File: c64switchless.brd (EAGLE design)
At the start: 22.8 x 44.1 mm, 12 parts, among them IC1 27C256, IC2 PIC12F629P, X1 B4B-ZR

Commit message: Revision + silkscreen text
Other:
- board text added: "B"
- board text added: "G"
- board text added: "Gnd"
- board text added: "LED"
- board text added: "R"
- board text added: "Revision 1"
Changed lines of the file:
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@@
 <setting verticaltext="up"/>
 </settings>
-<grid distance="0.05" unitdist="inch" unit="mm" style="lines" multiple="1" display="yes" altdistance="0.025" altunitdist="inch" altunit="inch"/>
+<grid distance="0.05" unitdist="inch" unit="inch" style="lines" multiple="1" display="yes" altdistance="0.025" altunitdist="inch" altunit="inch"/>
 <layers>
 <layer number="1" name="Top" color="4" fill="1" visible="yes" active="yes"/>
@@
 <text x="1.27" y="1.27" size="0.6096" layer="29" font="fixed">Quad Kernal Switch</text>
 <text x="5.715" y="5.5" size="0.6096" layer="21" rot="R340">RESET</text>
-<text x="11.43" y="0.5" size="0.6096" layer="21" rot="R70">Restore</text>
+<text x="13.335" y="3.04" size="0.6096" layer="21" rot="R70">Restore</text>
+<text x="13.97" y="1.27" size="0.6096" layer="23" font="fixed" rot="R90">LED</text>
+<text x="3.175" y="0.635" size="0.6096" layer="23" font="fixed">Revision 1</text>
+<text x="19.812" y="0.635" size="0.6096" layer="23" font="fixed">R</text>
+<text x="16.764" y="0.635" size="0.6096" layer="23" font="fixed">G</text>
+<text x="15.24" y="0.635" size="0.6096" layer="23" font="fixed">B</text>
+<text x="17.78" y="0.635" size="0.6096" layer="23" font="fixed">Gnd</text>
 </plain>
 <attributes>

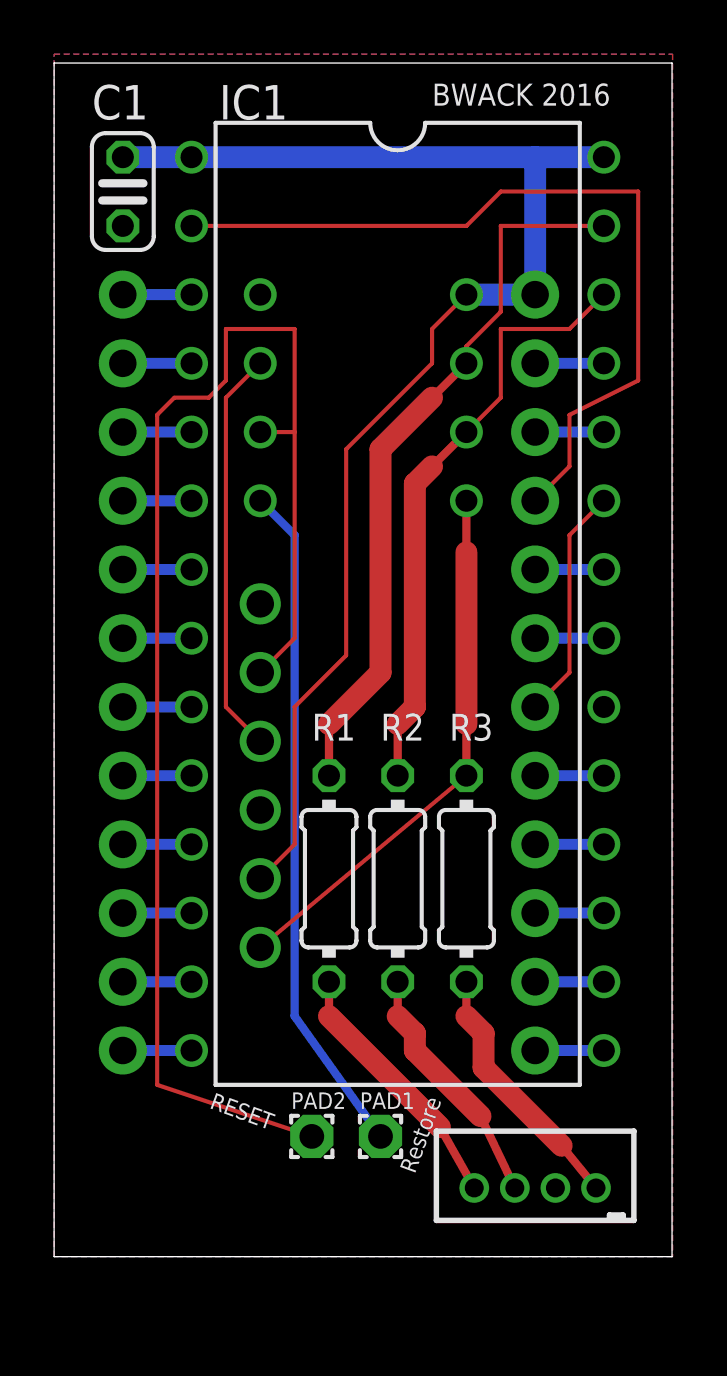
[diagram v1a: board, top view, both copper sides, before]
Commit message: swapped LED and RESTORE on GP2 and GP3
GP3 is the fekken input only pin
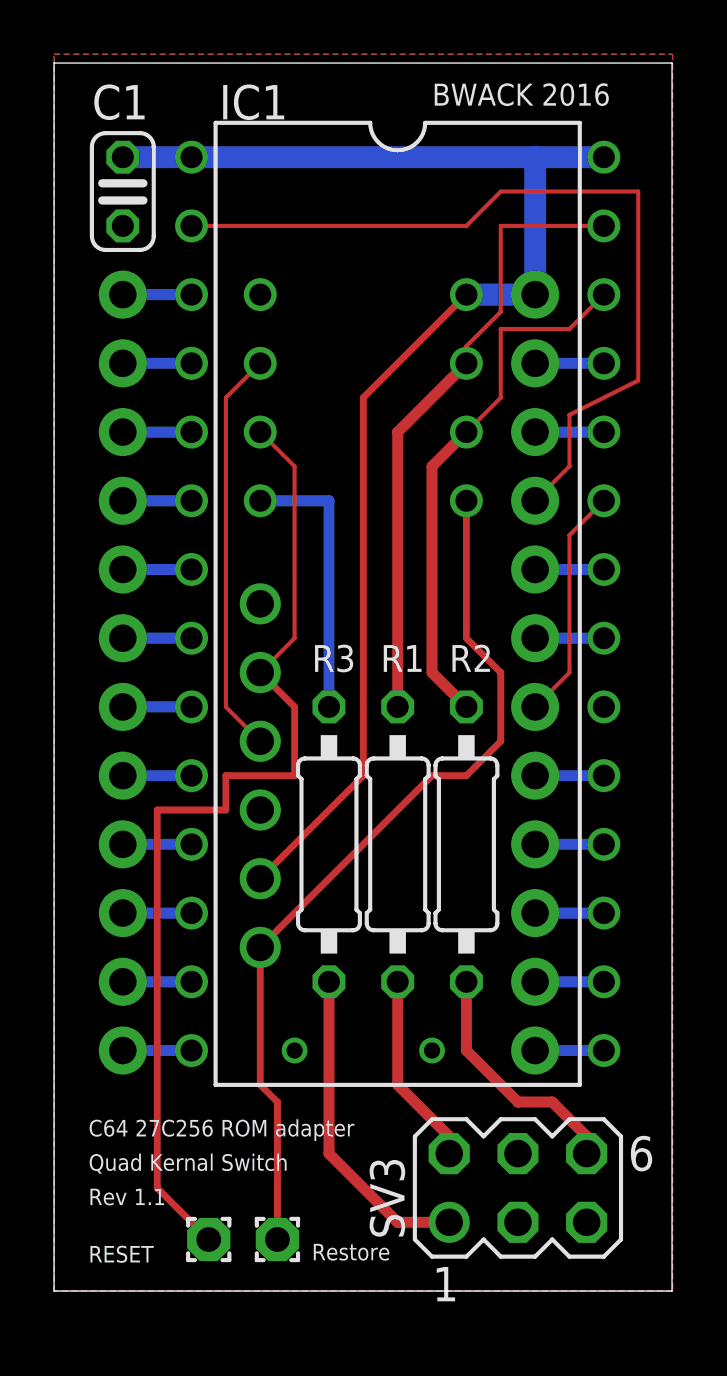
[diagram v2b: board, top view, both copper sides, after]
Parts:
- removed X1: B4B-ZR, con-jst:B4B-ZR
- added SV3: (no value), con-lstb:MA03-2
- R1, R2, R3: value 560 -> 2k; device rcl:0204/7 -> rcl:0207/10
- moved PAD2 5.39 mm to (5.71, 0.64)
- moved PAD1 5.39 mm to (8.26, 0.64)
- moved R3 5.24 mm to (10.2, 15.2)
- moved R2 2.84 mm to (15.2, 15.2)
- moved R1 2.84 mm to (12.7, 15.2)
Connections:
- removed net N$25: IC2.4, R3.2, U$1.1
- new net N$22: IC2.5, R3.2
- net #RESTORE: now also IC2.4, U$1.1; no longer IC2.5
- net BLUE: now also SV3.2; no longer X1.4
- net GND: now also SV3.3, SV3.4; no longer X1.2
- net GREEN: now also SV3.6; no longer X1.3
- net RED: now also SV3.1; no longer X1.1
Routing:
- net N$25: track 20.1 -> 0.00 mm
- net #INTRST: track 52.8 -> 37.3 mm
- net N$22: track 0.00 -> 10.2 mm
- net #RESTORE: track 25.0 -> 32.5 mm
- net A14: track 26.8 -> 23.2 mm
- net A13: track 22.4 -> 19.9 mm
- net BLUE: track 9.65 -> 7.14 mm
- net RED: track 9.53 -> 11.8 mm
- net GND: vias 0 -> 2
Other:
- board size 22.8 x 44.1 mm -> 22.8 x 45.4 mm
- board text added: "C64 27C256 ROM adapter"
- board text added: "Rev 1.1"
- board text removed: "27C256 ROM adapter"
- board text removed: "C64 Longboard"
- board text removed: "Revision 1"

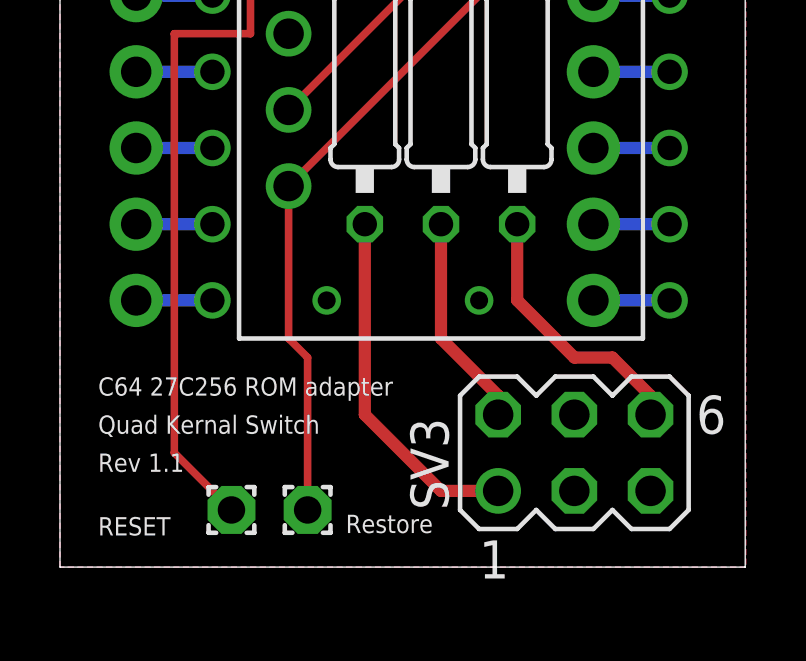
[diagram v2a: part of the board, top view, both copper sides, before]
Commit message: Sch+Layout changed to match RGB LEDs pinout
See readme.txt
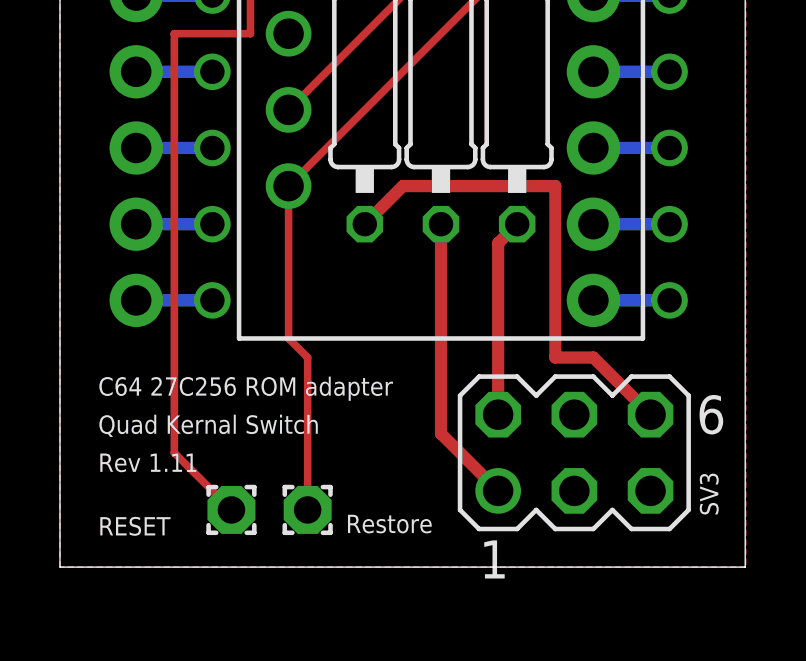
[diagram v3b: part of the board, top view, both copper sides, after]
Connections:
- net BLUE: now also SV3.1; no longer SV3.2
- net GREEN: now also SV3.2; no longer SV3.6
- net RED: now also SV3.6; no longer SV3.1
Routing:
- net RED: track 11.8 -> 16.6 mm
- net BLUE: track 7.14 -> 9.68 mm
- net GREEN: track 8.94 -> 6.61 mm
- net GND: vias 2 -> 0
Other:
- board text added: "BLUE"
- board text added: "GND"
- board text added: "GREEN"
- board text added: "RED"
- board text added: "RGB LEDs"
- board text added: "Rev 1.11"
- board text removed: "B"
- board text removed: "G"
- board text removed: "Gnd"
- board text removed: "LED"
- board text removed: "R"
- board text removed: "Rev 1.1"
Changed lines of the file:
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@@
 <setting verticaltext="up"/>
 </settings>
-<grid distance="0.05" unitdist="inch" unit="inch" style="lines" multiple="1" display="yes" altdistance="0.025" altunitdist="inch" altunit="inch"/>
+<grid distance="0.05" unitdist="inch" unit="inch" style="lines" multiple="1" display="yes" altdistance="0.0125" altunitdist="inch" altunit="inch"/>
 <layers>
 <layer number="1" name="Top" color="4" fill="1" visible="yes" active="yes"/>
@@
 <text x="1.27" y="-0.215" size="0.6096" layer="21">RESET</text>
 <text x="9.525" y="-0.135" size="0.6096" layer="21">Restore</text>
-<text x="13.97" y="1.27" size="0.6096" layer="23" font="fixed" rot="R90">LED</text>
-<text x="1.27" y="1.905" size="0.6096" layer="21" font="fixed">Rev 1.1</text>
-<text x="19.812" y="0.635" size="0.6096" layer="23" font="fixed">R</text>
-<text x="16.764" y="0.635" size="0.6096" layer="23" font="fixed">G</text>
-<text x="15.24" y="0.635" size="0.6096" layer="23" font="fixed">B</text>
-<text x="17.78" y="0.635" size="0.6096" layer="23" font="fixed">Gnd</text>
+<text x="19.05" y="0" size="0.6096" layer="23" font="fixed" rot="R180">RGB LEDs</text>
+<text x="1.27" y="1.905" size="0.6096" layer="21" font="fixed">Rev 1.11</text>
+<text x="18.8595" y="5.3975" size="0.6096" layer="23" font="fixed">RED</text>
+<text x="13.2715" y="5.3975" size="0.6096" layer="23" font="fixed">GREEN</text>
+<text x="13.0175" y="0.9525" size="0.6096" layer="23" font="fixed" rot="R90">BLUE</text>
+<text x="16.51" y="5.3975" size="0.6096" layer="23" font="fixed">GND</text>
 </plain>
 <attributes>
@@
 <attribute name="MF" value="" x="17.145" y="2.54" size="1.778" layer="27" display="off"/>
 <attribute name="OC_FARNELL" value="unknown" x="17.145" y="2.54" size="1.778" layer="27" display="off"/>
-<attribute name="NAME" x="12.954" y="0.635" size="1.27" layer="25" ratio="10" rot="R90"/>
+<attribute name="NAME" x="21.336" y="1.905" size="0.6096" layer="25" ratio="10" rot="R270"/>
 <attribute name="VALUE" x="15.875" y="-1.651" size="1.27" layer="27" ratio="10"/>
 </element>
@@
 <contactref element="SV3" pad="3"/>
 <contactref element="SV3" pad="4"/>
-<via x="8.89" y="7.62" extent="1-16" drill="0.6"/>
-<via x="13.97" y="7.62" extent="1-16" drill="0.6"/>
 </signal>
 <signal name="VCC">
@@
 <wire x1="12.7" y1="30.48" x2="15.24" y2="33.02" width="0.4064" layer="1"/>
 </signal>
-<signal name="GREEN">
-<contactref element="R2" pad="1"/>
-<contactref element="SV3" pad="6"/>
-<wire x1="15.24" y1="10.16" x2="15.24" y2="7.62" width="0.4064" layer="1"/>
-<wire x1="15.24" y1="7.62" x2="17.145" y2="5.715" width="0.4064" layer="1"/>
-<wire x1="19.685" y1="3.81" x2="19.685" y2="4.445" width="0.4064" layer="1"/>
-<wire x1="19.685" y1="4.445" x2="18.415" y2="5.715" width="0.4064" layer="1"/>
-<wire x1="18.415" y1="5.715" x2="17.145" y2="5.715" width="0.4064" layer="1"/>
-</signal>
 <signal name="BLUE">
 <contactref element="R1" pad="1"/>
-<contactref element="SV3" pad="2"/>
-<wire x1="14.605" y1="3.81" x2="14.605" y2="4.445" width="0.4064" layer="1"/>
-<wire x1="14.605" y1="4.445" x2="12.7" y2="6.35" width="0.4064" layer="1"/>
-<wire x1="12.7" y1="10.16" x2="12.7" y2="6.35" width="0.4064" layer="1"/>
+<contactref element="SV3" pad="1"/>
+<wire x1="12.7" y1="10.16" x2="12.7" y2="3.175" width="0.4064" layer="1"/>
+<wire x1="14.605" y1="1.27" x2="12.7" y2="3.175" width="0.4064" layer="1"/>
 </signal>
 <signal name="N$1">
@@
 <signal name="RED">
 <contactref element="R3" pad="1"/>
-<contactref element="SV3" pad="1"/>
-<wire x1="14.605" y1="1.27" x2="12.7" y2="1.27" width="0.4064" layer="1"/>
-<wire x1="12.7" y1="1.27" x2="10.16" y2="3.81" width="0.4064" layer="1"/>
-<wire x1="10.16" y1="3.81" x2="10.16" y2="10.16" width="0.4064" layer="1"/>
+<contactref element="SV3" pad="6"/>
+<wire x1="10.16" y1="10.16" x2="11.43" y2="11.43" width="0.4064" layer="1"/>
+<wire x1="11.43" y1="11.43" x2="16.51" y2="11.43" width="0.4064" layer="1"/>
+<wire x1="16.51" y1="11.43" x2="16.51" y2="5.715" width="0.4064" layer="1"/>
+<wire x1="19.685" y1="3.81" x2="17.78" y2="5.715" width="0.4064" layer="1"/>
+<wire x1="17.78" y1="5.715" x2="16.51" y2="5.715" width="0.4064" layer="1"/>
 </signal>
 <signal name="N$22">
@@
 <wire x1="10.16" y1="27.94" x2="10.16" y2="20.32" width="0.4064" layer="16"/>
 </signal>
+<signal name="GREEN">
+<contactref element="R2" pad="1"/>
+<contactref element="SV3" pad="2"/>
+<wire x1="15.24" y1="10.16" x2="14.605" y2="9.525" width="0.4064" layer="1"/>
+<wire x1="14.605" y1="9.525" x2="14.605" y2="3.81" width="0.4064" layer="1"/>
+</signal>
 </signals>
